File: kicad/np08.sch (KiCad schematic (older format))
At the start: 18 parts, among them P1 USB_B, P10 CONN_01X02, P11 CONN_01X02, P12 analog, P13 GND, P14 +5V, P2 CONN_01X04, SW1 SW_PUSH, Y1 Crystal

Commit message: cambios menores
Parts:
- D1: symbol LED -> LED-RESCUE-np08
- P1: symbol USB_B -> USB_B-RESCUE-np08
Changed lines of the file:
@@
 EESchema Schematic File Version 2
+LIBS:np08-rescue
 LIBS:power
 LIBS:device
@@
 $EndComp
 $Comp
-L LED D1
+L LED-RESCUE-np08 D1
 U 1 1 579A397D
 P 3450 2450
@@
 	7550 3300 7650 3300
 $Comp
-L USB_B P1
+L USB_B-RESCUE-np08 P1
 U 1 1 579A4922
 P 2950 4650

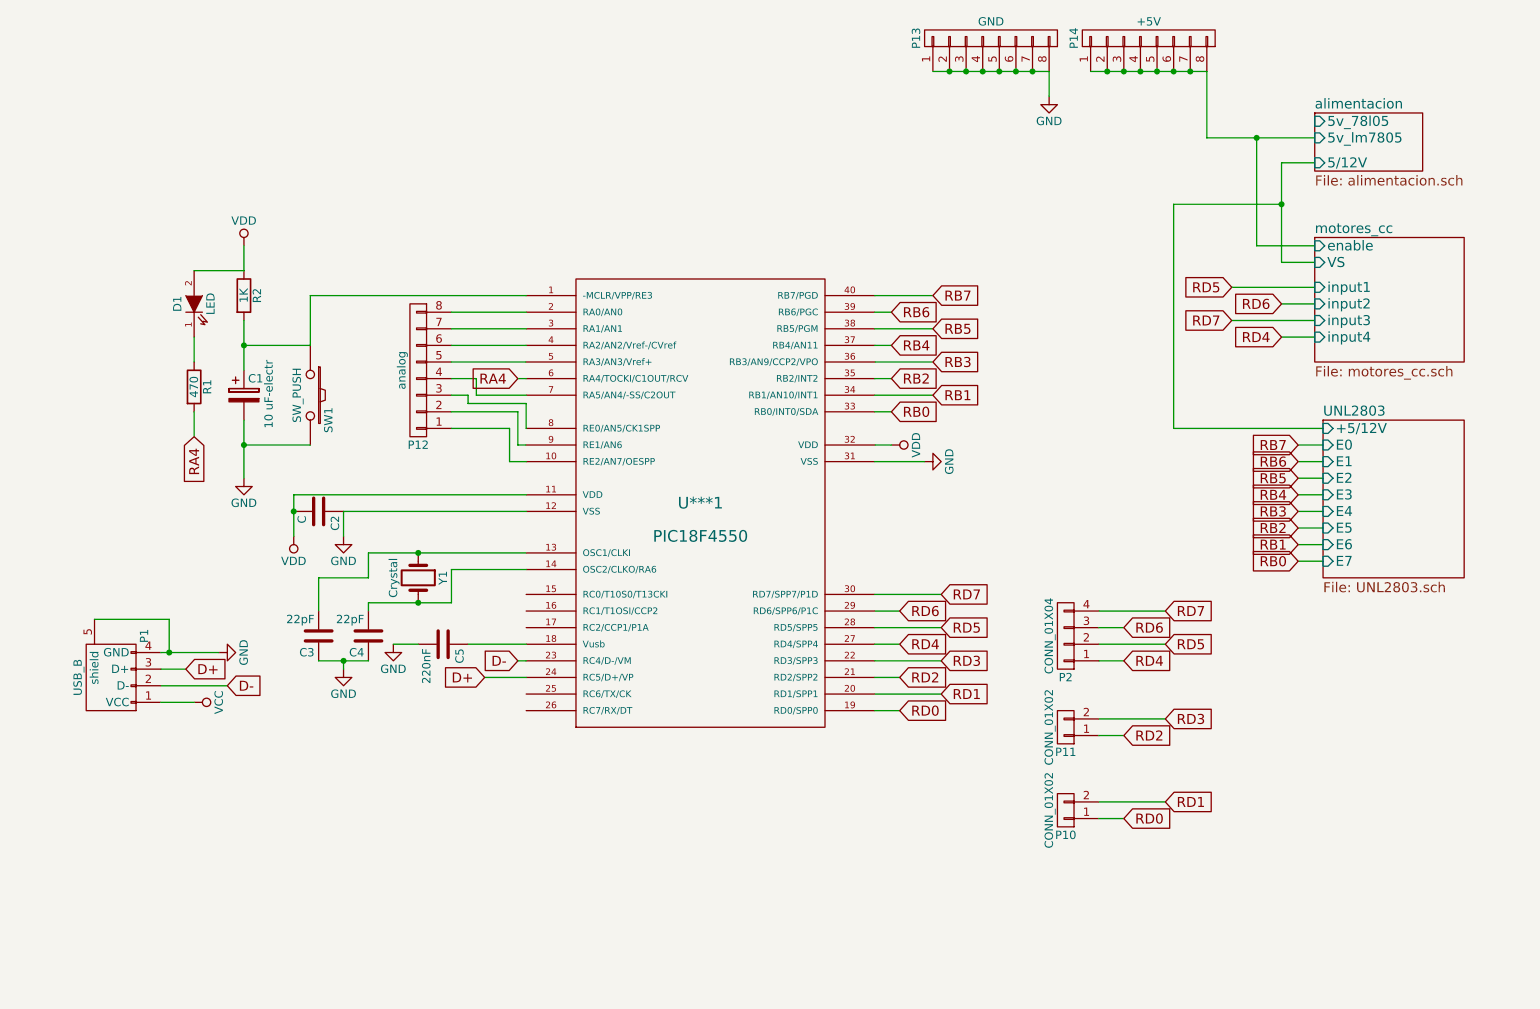
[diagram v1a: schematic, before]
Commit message: cambios en la placa np08
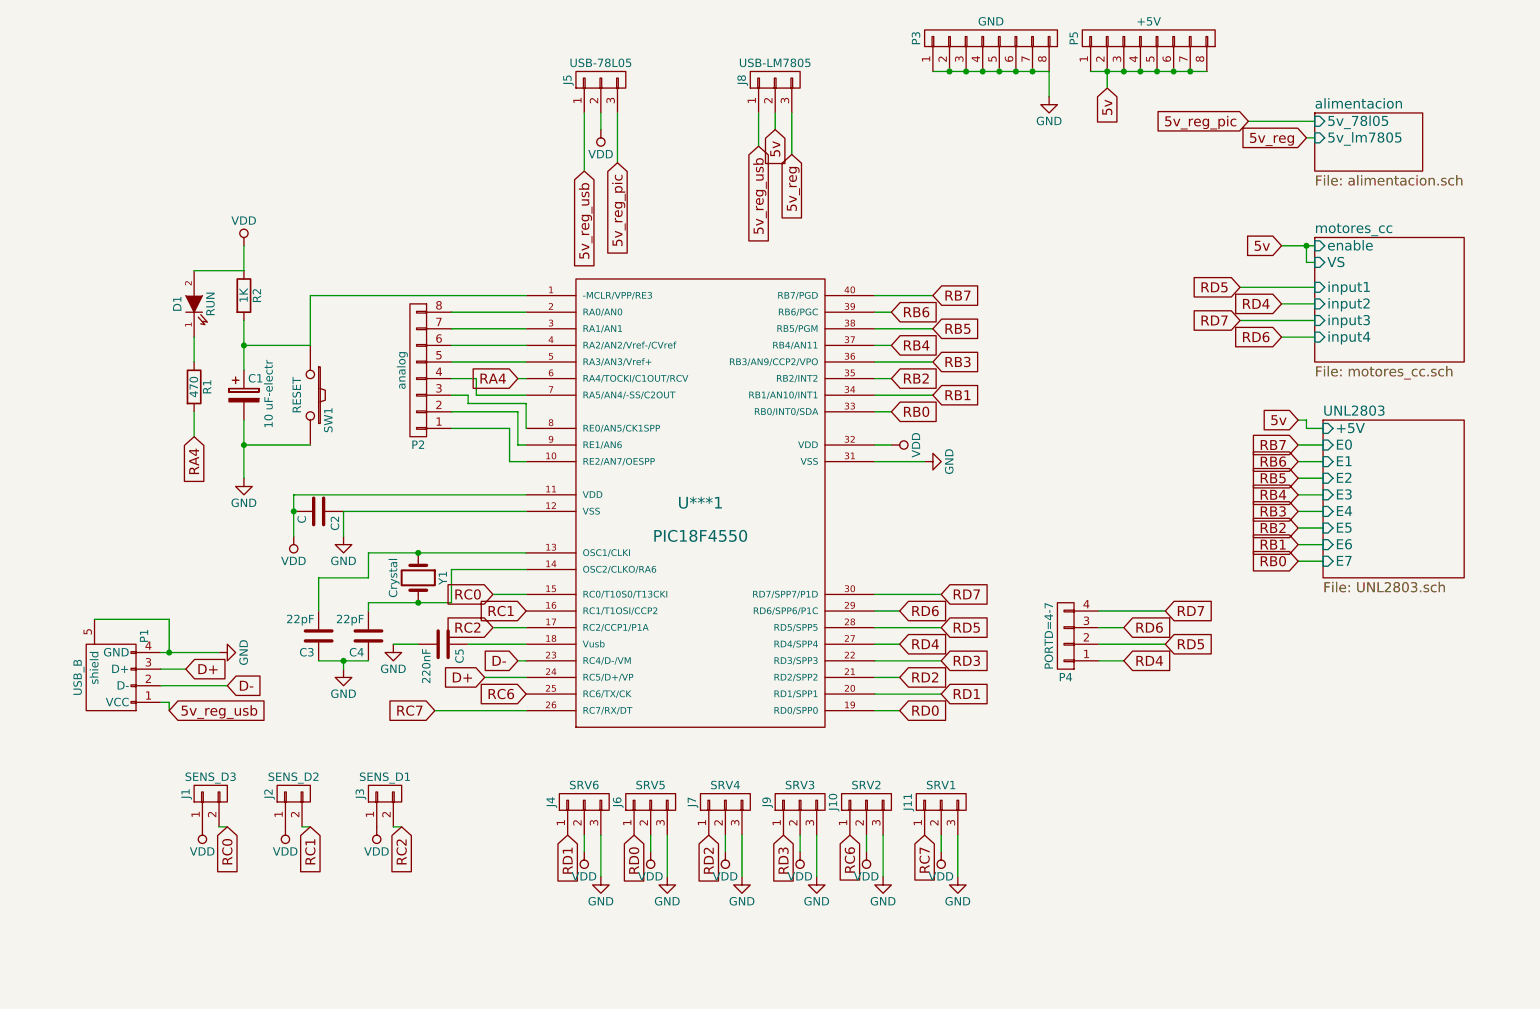
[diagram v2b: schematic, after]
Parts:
- removed P10, P11: CONN_01X02, Pin_Headers:Pin_Header_Straight_1x02, symbol CONN_01X02
- added J1: SENS_D3, Pin_Headers:Pin_Header_Straight_1x02_Pitch2.54mm, symbol CONN_01X02
- added J10: SRV2, Pin_Headers:Pin_Header_Straight_1x03_Pitch2.54mm, symbol CONN_01X03
- added J11: SRV1, Pin_Headers:Pin_Header_Straight_1x03_Pitch2.54mm, symbol CONN_01X03
- added J2: SENS_D2, Pin_Headers:Pin_Header_Straight_1x02_Pitch2.54mm, symbol CONN_01X02
- added J3: SENS_D1, Pin_Headers:Pin_Header_Straight_1x02_Pitch2.54mm, symbol CONN_01X02
- added J4: SRV6, Pin_Headers:Pin_Header_Straight_1x03_Pitch2.54mm, symbol CONN_01X03
- added J5: USB-78L05, Pin_Headers:Pin_Header_Straight_1x03_Pitch2.54mm, symbol CONN_01X03
- added J6: SRV5, Pin_Headers:Pin_Header_Straight_1x03_Pitch2.54mm, symbol CONN_01X03
- added J7: SRV4, Pin_Headers:Pin_Header_Straight_1x03_Pitch2.54mm, symbol CONN_01X03
- added J8: USB-LM7805, Pin_Headers:Pin_Header_Straight_1x03_Pitch2.54mm, symbol CONN_01X03
- added J9: SRV3, Pin_Headers:Pin_Header_Straight_1x03_Pitch2.54mm, symbol CONN_01X03
- C1: footprint Capacitors_ThroughHole:C_Radial_D5_L6_P2.5 -> Capacitors_THT:CP_Radial_D6.3mm_P2.50mm
- C2, C3, C4, C5: footprint Capacitors_ThroughHole:C_Disc_D3_P2.5 -> Capacitors_THT:C_Disc_D3.4mm_W2.1mm_P2.50mm
- D1: value LED -> RUN; footprint LEDs:LED-5MM -> LEDs:LED_D5.0mm
- P1: footprint Connect:USB_B -> Connectors:USB_B
- P2: renamed from P12; footprint Pin_Headers:Pin_Header_Straight_1x08 -> Pin_Headers:Pin_Header_Straight_1x08_Pitch2.54mm
- P3: renamed from P13; footprint Pin_Headers:Pin_Header_Straight_1x08 -> Pin_Headers:Pin_Header_Straight_1x08_Pitch2.54mm
- P4: renamed from P2; value CONN_01X04 -> PORTD=4-7; footprint Pin_Headers:Pin_Header_Straight_1x04 -> Pin_Headers:Pin_Header_Straight_1x04_Pitch2.54mm
- P5: renamed from P14; footprint Pin_Headers:Pin_Header_Straight_1x08 -> Pin_Headers:Pin_Header_Straight_1x08_Pitch2.54mm
- R1, R2: footprint Resistors_ThroughHole:Resistor_Horizontal_RM15mm -> Resistors_THT:R_Axial_DIN0411_L9.9mm_D3.6mm_P12.70mm_Horizontal
- SW1: value SW_PUSH -> RESET; footprint Buttons_Switches_ThroughHole:SW_PUSH-12mm -> Buttons_Switches_THT:SW_PUSH_6mm_h5mm
- U***1: footprint Housings_DIP:DIP-40_W15.24mm -> Housings_DIP:DIP-40_W15.24mm_LongPads
- Y1: footprint Crystals:Crystal_HC50-U_Vertical -> Crystals:Crystal_HC50_Vertical
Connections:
- net GND: now also J10.3 (P3), J11.3 (P3), J4.3 (P3), J6.3 (P3), J7.3 (P3), J9.3 (P3)
- net RD0: now also J6.1 (P1)
- net RD1: now also J4.1 (P1)
- net RD2: now also J7.1 (P1)
- net RD3: now also J9.1 (P1)
- net VDD: now also J1.1 (P1), J10.2 (P2), J11.2 (P2), J2.1 (P1), J3.1 (P1), J4.2 (P2), J5.2 (P2), J6.2 (P2), J7.2 (P2), J9.2 (P2)
- net RC0: now reaches U***1.15 (RC0/T10S0/T13CKI)
- net RC0: now also J1.2 (P2)
- net RC1: now reaches U***1.16 (RC1/T1OSI/CCP2)
- net RC1: now also J2.2 (P2)
- net RC2: now reaches U***1.17 (RC2/CCP1/P1A)
- net RC2: now also J3.2 (P2)
- net RC6: now reaches U***1.25 (RC6/TX/CK)
- net RC6: now also J10.1 (P1)
- net RC7: now reaches U***1.26 (RC7/RX/DT)
- net RC7: now also J11.1 (P1)
- net VCC renamed 5v_reg_usb
- net 5v_reg_usb: now also J5.1 (P1), J8.1 (P1)
- net alimentacion/5v_lm7805 renamed 5v
- net 5v: now also J8.2 (P2)
- new net 5v_reg: J8.3 (P3)
- new net 5v_reg_pic: J5.3 (P3)

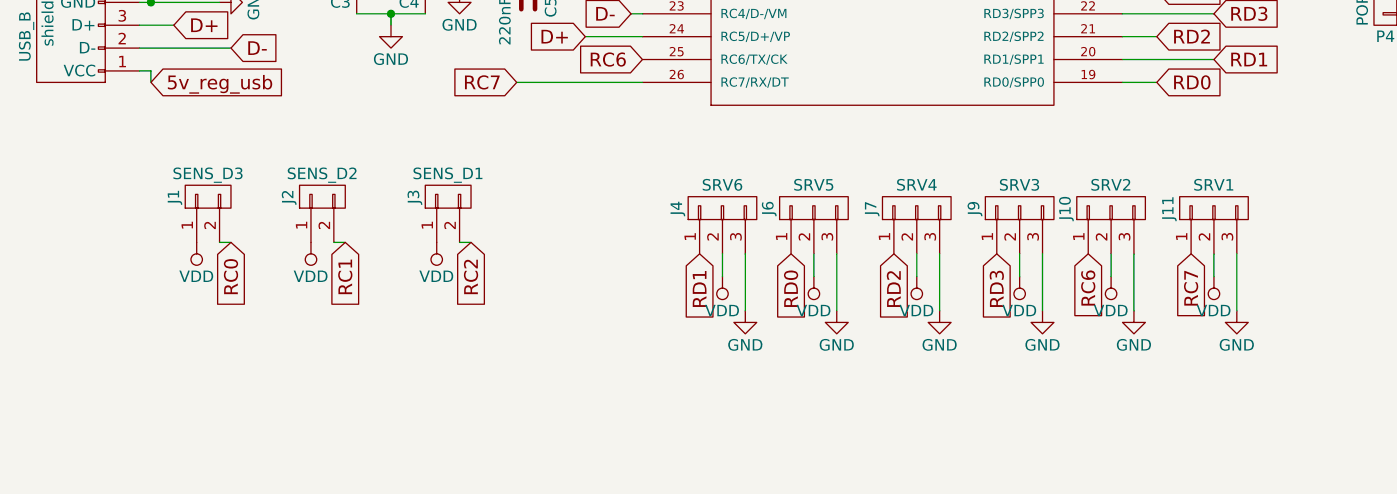
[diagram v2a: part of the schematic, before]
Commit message: arreglando la fuente de alimentación, los servos estaban conectados al 78l05
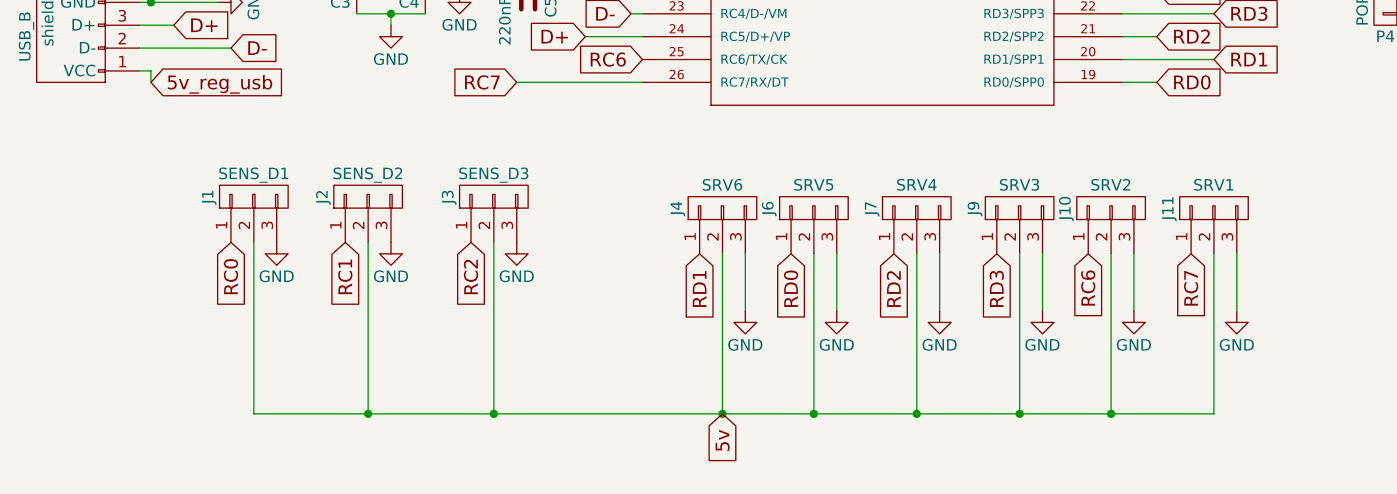
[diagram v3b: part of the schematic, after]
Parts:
- removed J1: SENS_D3, Pin_Headers:Pin_Header_Straight_1x02_Pitch2.54mm, symbol CONN_01X02
- removed J2: SENS_D2, Pin_Headers:Pin_Header_Straight_1x02_Pitch2.54mm, symbol CONN_01X02
- removed J3: SENS_D1, Pin_Headers:Pin_Header_Straight_1x02_Pitch2.54mm, symbol CONN_01X02
- added J1: SENS_D1, Pin_Headers:Pin_Header_Straight_1x03_Pitch2.54mm, symbol CONN_01X03
- added J2: SENS_D2, Pin_Headers:Pin_Header_Straight_1x03_Pitch2.54mm, symbol CONN_01X03
- added J3: SENS_D3, Pin_Headers:Pin_Header_Straight_1x03_Pitch2.54mm, symbol CONN_01X03
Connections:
- net 5v: now also J10.2 (P2), J11.2 (P2), J4.2 (P2), J6.2 (P2), J7.2 (P2), J9.2 (P2), J1.2 (P2), J2.2 (P2), J3.2 (P2)
- net GND: now also J1.3 (P3), J2.3 (P3), J3.3 (P3)
- net RC0: now also J1.1 (P1)
- net RC1: now also J2.1 (P1)
- net RC2: now also J3.1 (P1)
- net VDD: no longer J10.2 (P2), J11.2 (P2), J4.2 (P2), J6.2 (P2), J7.2 (P2), J9.2 (P2)
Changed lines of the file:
@@
 	1    0    0    -1
 $EndComp
-$Comp
-L VDD #PWR013
-U 1 1 59A9A2AC
-P 7950 5750
-F 0 "#PWR013" H 7950 5600 50  0001 C CNN
-F 1 "VDD" H 7950 5900 50  0000 C CNN
-F 2 "" H 7950 5750 50  0000 C CNN
-F 3 "" H 7950 5750 50  0000 C CNN
-	1    7950 5750
-	-1   0    0    1
-$EndComp
-Wire Wire Line
-	7950 5750 7950 5650
+Wire Wire Line
+	7950 6350 7950 5650
 Wire Wire Line
 	8050 5900 8050 5650
@@
 $EndComp
 $Comp
-L GND #PWR014
+L GND #PWR013
 U 1 1 59A9ACF6
 P 7600 5900
-F 0 "#PWR014" H 7600 5650 50  0001 C CNN
+F 0 "#PWR013" H 7600 5650 50  0001 C CNN
 F 1 "GND" H 7600 5750 50  0000 C CNN
 F 2 "" H 7600 5900 50  0001 C CNN
@@
 	1    0    0    -1
 $EndComp
-$Comp
-L VDD #PWR015
-U 1 1 59A9ACFC
-P 7500 5750
-F 0 "#PWR015" H 7500 5600 50  0001 C CNN
-F 1 "VDD" H 7500 5900 50  0000 C CNN
-F 2 "" H 7500 5750 50  0000 C CNN
-F 3 "" H 7500 5750 50  0000 C CNN
-	1    7500 5750
-	-1   0    0    1
-$EndComp
-Wire Wire Line
-	7500 5750 7500 5650
+Wire Wire Line
+	7500 5650 7500 6350
 Wire Wire Line
 	7600 5900 7600 5650
@@
 $EndComp
 $Comp
-L GND #PWR016
+L GND #PWR014
 U 1 1 59A9B0AE
 P 7200 5900
-F 0 "#PWR016" H 7200 5650 50  0001 C CNN
+F 0 "#PWR014" H 7200 5650 50  0001 C CNN
 F 1 "GND" H 7200 5750 50  0000 C CNN
 F 2 "" H 7200 5900 50  0001 C CNN
@@
 	1    0    0    -1
 $EndComp
-$Comp
-L VDD #PWR017
-U 1 1 59A9B0B4
-P 7100 5750
-F 0 "#PWR017" H 7100 5600 50  0001 C CNN
-F 1 "VDD" H 7100 5900 50  0000 C CNN
-F 2 "" H 7100 5750 50  0000 C CNN
-F 3 "" H 7100 5750 50  0000 C CNN
-	1    7100 5750
-	-1   0    0    1
-$EndComp
-Wire Wire Line
-	7100 5750 7100 5650
+Wire Wire Line
+	7100 5650 7100 6350
 Wire Wire Line
 	7200 5900 7200 5650
@@
 $EndComp
 $Comp
-L GND #PWR018
+L GND #PWR015
 U 1 1 59A9B2F2
 P 6750 5900
-F 0 "#PWR018" H 6750 5650 50  0001 C CNN
+F 0 "#PWR015" H 6750 5650 50  0001 C CNN
 F 1 "GND" H 6750 5750 50  0000 C CNN
 F 2 "" H 6750 5900 50  0001 C CNN
@@
 	1    0    0    -1
 $EndComp
-$Comp
-L VDD #PWR019
-U 1 1 59A9B2F8
-P 6650 5750
-F 0 "#PWR019" H 6650 5600 50  0001 C CNN
-F 1 "VDD" H 6650 5900 50  0000 C CNN
-F 2 "" H 6650 5750 50  0000 C CNN
-F 3 "" H 6650 5750 50  0000 C CNN
-	1    6650 5750
-	-1   0    0    1
-$EndComp
-Wire Wire Line
-	6650 5750 6650 5650
+Wire Wire Line
+	6650 5650 6650 6350
 Wire Wire Line
 	6750 5900 6750 5650
@@
 $EndComp
 $Comp
-L GND #PWR020
+L GND #PWR016
 U 1 1 59A9B541
 P 6300 5900
-F 0 "#PWR020" H 6300 5650 50  0001 C CNN
+F 0 "#PWR016" H 6300 5650 50  0001 C CNN
 F 1 "GND" H 6300 5750 50  0000 C CNN
 F 2 "" H 6300 5900 50  0001 C CNN
@@
 	1    0    0    -1
 $EndComp
-$Comp
-L VDD #PWR021
-U 1 1 59A9B547
-P 6200 5750
-F 0 "#PWR021" H 6200 5600 50  0001 C CNN
-F 1 "VDD" H 6200 5900 50  0000 C CNN
-F 2 "" H 6200 5750 50  0000 C CNN
-F 3 "" H 6200 5750 50  0000 C CNN
-	1    6200 5750
-	-1   0    0    1
-$EndComp
-Wire Wire Line
-	6200 5750 6200 5650
+Wire Wire Line
+	6200 5650 6200 6350
 Wire Wire Line
 	6300 5900 6300 5650
@@
 $EndComp
 $Comp
-L GND #PWR022
+L GND #PWR017
 U 1 1 59A9B6B9
 P 5900 5900
-F 0 "#PWR022" H 5900 5650 50  0001 C CNN
+F 0 "#PWR017" H 5900 5650 50  0001 C CNN
 F 1 "GND" H 5900 5750 50  0000 C CNN
 F 2 "" H 5900 5900 50  0001 C CNN
@@
 	1    0    0    -1
 $EndComp
-$Comp
-L VDD #PWR023
-U 1 1 59A9B6BF
-P 5800 5750
-F 0 "#PWR023" H 5800 5600 50  0001 C CNN
-F 1 "VDD" H 5800 5900 50  0000 C CNN
-F 2 "" H 5800 5750 50  0000 C CNN
-F 3 "" H 5800 5750 50  0000 C CNN
-	1    5800 5750
-	-1   0    0    1
-$EndComp
-Wire Wire Line
-	5800 5750 5800 5650
+Wire Wire Line
+	5800 5650 5800 6350
 Wire Wire Line
 	5900 5900 5900 5650
@@
 Text GLabel 4700 5600 3    60   Input ~ 0
 RC2
-$Comp
-L CONN_01X02 J3
-U 1 1 59A9DC48
-P 4600 5400
-F 0 "J3" H 4600 5550 50  0000 C CNN
-F 1 "SENS_D1" V 4700 5400 50  0000 C CNN
-F 2 "Pin_Headers:Pin_Header_Straight_1x02_Pitch2.54mm" H 4600 5400 50  0001 C CNN
-F 3 "" H 4600 5400 50  0001 C CNN
-	1    4600 5400
-	0    -1   -1   0
-$EndComp
-$Comp
-L CONN_01X02 J2
-U 1 1 59A9DD36
-P 4050 5400
-F 0 "J2" H 4050 5550 50  0000 C CNN
-F 1 "SENS_D2" V 4150 5400 50  0000 C CNN
-F 2 "Pin_Headers:Pin_Header_Straight_1x02_Pitch2.54mm" H 4050 5400 50  0001 C CNN
-F 3 "" H 4050 5400 50  0001 C CNN
-	1    4050 5400
-	0    -1   -1   0
-$EndComp
-$Comp
-L CONN_01X02 J1
-U 1 1 59A9DE14
-P 3550 5400
-F 0 "J1" H 3550 5550 50  0000 C CNN
-F 1 "SENS_D3" V 3650 5400 50  0000 C CNN
-F 2 "Pin_Headers:Pin_Header_Straight_1x02_Pitch2.54mm" H 3550 5400 50  0001 C CNN
-F 3 "" H 3550 5400 50  0001 C CNN
-	1    3550 5400
-	0    -1   -1   0
-$EndComp
-$Comp
-L VDD #PWR024
-U 1 1 59A9E38F
-P 4550 5600
-F 0 "#PWR024" H 4550 5450 50  0001 C CNN
-F 1 "VDD" H 4550 5750 50  0000 C CNN
-F 2 "" H 4550 5600 50  0000 C CNN
-F 3 "" H 4550 5600 50  0000 C CNN
-	1    4550 5600
-	-1   0    0    1
-$EndComp
-$Comp
-L VDD #PWR025
-U 1 1 59A9E678
-P 4000 5600
-F 0 "#PWR025" H 4000 5450 50  0001 C CNN
-F 1 "VDD" H 4000 5750 50  0000 C CNN
-F 2 "" H 4000 5600 50  0000 C CNN
-F 3 "" H 4000 5600 50  0000 C CNN
-	1    4000 5600
-	-1   0    0    1
-$EndComp
-$Comp
-L VDD #PWR026
-U 1 1 59A9E73A
-P 3500 5600
-F 0 "#PWR026" H 3500 5450 50  0001 C CNN
-F 1 "VDD" H 3500 5750 50  0000 C CNN
-F 2 "" H 3500 5600 50  0000 C CNN
-F 3 "" H 3500 5600 50  0000 C CNN
-	1    3500 5600
-	-1   0    0    1
-$EndComp
-Wire Wire Line
-	4650 5600 4700 5600
-Wire Wire Line
-	4100 5600 4150 5600
-Wire Wire Line
-	3600 5600 3650 5600
+Text GLabel 5800 6350 3    60   Input ~ 0
+5v
+$Comp
+L CONN_01X03 J3
+U 1 1 59C17178
+P 4800 5400
+F 0 "J3" H 4800 5600 50  0000 C CNN
+F 1 "SENS_D3" V 4900 5400 50  0000 C CNN
+F 2 "Pin_Headers:Pin_Header_Straight_1x03_Pitch2.54mm" H 4800 5400 50  0001 C CNN
+F 3 "" H 4800 5400 50  0001 C CNN
+	1    4800 5400
+	0    -1   -1   0
+$EndComp
+$Comp
+L CONN_01X03 J2
+U 1 1 59C1726D
+P 4250 5400
+F 0 "J2" H 4250 5600 50  0000 C CNN
+F 1 "SENS_D2" V 4350 5400 50  0000 C CNN
+F 2 "Pin_Headers:Pin_Header_Straight_1x03_Pitch2.54mm" H 4250 5400 50  0001 C CNN
+F 3 "" H 4250 5400 50  0001 C CNN
+	1    4250 5400
+	0    -1   -1   0
+$EndComp
+$Comp
+L CONN_01X03 J1
+U 1 1 59C17347
+P 3750 5400
+F 0 "J1" H 3750 5600 50  0000 C CNN
+F 1 "SENS_D1" V 3850 5400 50  0000 C CNN
+F 2 "Pin_Headers:Pin_Header_Straight_1x03_Pitch2.54mm" H 3750 5400 50  0001 C CNN
+F 3 "" H 3750 5400 50  0001 C CNN
+	1    3750 5400
+	0    -1   -1   0
+$EndComp
+$Comp
+L GND #PWR018
+U 1 1 59C178FB
+P 4900 5600
+F 0 "#PWR018" H 4900 5350 50  0001 C CNN
+F 1 "GND" H 4900 5450 50  0000 C CNN
+F 2 "" H 4900 5600 50  0001 C CNN
+F 3 "" H 4900 5600 50  0001 C CNN
+	1    4900 5600
+	1    0    0    -1
+$EndComp
+$Comp
+L GND #PWR019
+U 1 1 59C179BD
+P 4350 5600
+F 0 "#PWR019" H 4350 5350 50  0001 C CNN
+F 1 "GND" H 4350 5450 50  0000 C CNN
+F 2 "" H 4350 5600 50  0001 C CNN
+F 3 "" H 4350 5600 50  0001 C CNN
+	1    4350 5600
+	1    0    0    -1
+$EndComp
+$Comp
+L GND #PWR020
+U 1 1 59C17A7F
+P 3850 5600
+F 0 "#PWR020" H 3850 5350 50  0001 C CNN
+F 1 "GND" H 3850 5450 50  0000 C CNN
+F 2 "" H 3850 5600 50  0001 C CNN
+F 3 "" H 3850 5600 50  0001 C CNN
+	1    3850 5600
+	1    0    0    -1
+$EndComp
+Wire Wire Line
+	3750 6350 7950 6350
+Connection ~ 7500 6350
+Connection ~ 7100 6350
+Connection ~ 6650 6350
+Connection ~ 6200 6350
+Wire Wire Line
+	3750 6350 3750 5600
+Connection ~ 5800 6350
+Wire Wire Line
+	4250 5600 4250 6350
+Connection ~ 4250 6350
+Wire Wire Line
+	4800 5600 4800 6350
+Connection ~ 4800 6350
 $EndSCHEMATC
